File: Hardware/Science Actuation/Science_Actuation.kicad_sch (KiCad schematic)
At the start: 79 parts, among them J2 RJ45_LED_Shielded, SW1 SW_Push, SW2 SW_Push, SW3 SW_Push, SW4 SW_Push, SW5 SW_Push, SW6 SW_Push, SW7 SW_SPDT, U2 OKI, U2 Teensy4.1_DEV-16771, U3 VNH7070AS, U4 VNH7070AS, U5 VNH7070AS, U6 VNH7070AS

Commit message: Add more caps to VNH and expand 12V plane
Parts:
- added C13, C14, C15, C16: 10uF, Capacitor_SMD:C_0603_1608Metric_Pad1.08x0.95mm_HandSolder, symbol Device:C
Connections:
- net +12V: now also C13.1, C14.1, C15.1, C16.1
- net GND: now also C13.2, C14.2, C15.2, C16.2
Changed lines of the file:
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@@
     (stroke (width 0) (type default))
   )
+  (wire (pts (xy 72.39 208.28) (xy 72.39 207.01))
+    (stroke (width 0) (type default))
+  )
   (wire (pts (xy 190.5 156.21) (xy 190.5 157.48))
     (stroke (width 0) (type default))
@@
     (stroke (width 0) (type default))
   )
+  (wire (pts (xy 62.23 102.87) (xy 64.77 102.87))
+    (stroke (width 0) (type default))
+  )
   (wire (pts (xy 27.94 67.31) (xy 46.99 67.31))
     (stroke (width 0) (type default))
@@
     (stroke (width 0) (type default))
   )
+  (wire (pts (xy 73.66 156.21) (xy 73.66 154.94))
+    (stroke (width 0) (type default))
+  )
   (wire (pts (xy 76.2 285.75) (xy 76.2 287.02))
     (stroke (width 0) (type default))
@@
     (stroke (width 0) (type default))
   )
+  (wire (pts (xy 60.96 207.01) (xy 63.5 207.01))
+    (stroke (width 0) (type default))
+  )
   (wire (pts (xy 152.4 267.97) (xy 152.4 276.86))
     (stroke (width 0) (type default))
@@
     (stroke (width 0) (type default))
   )
+  (wire (pts (xy 62.23 154.94) (xy 64.77 154.94))
+    (stroke (width 0) (type default))
+  )
   (wire (pts (xy 143.51 113.03) (xy 146.05 113.03))
     (stroke (width 0) (type default))
@@
     (stroke (width 0) (type default))
   )
+  (wire (pts (xy 72.39 207.01) (xy 71.12 207.01))
+    (stroke (width 0) (type default))
+  )
   (wire (pts (xy 290.83 87.63) (xy 293.37 87.63))
     (stroke (width 0) (type default))
@@
     (stroke (width 0) (type default))
   )
+  (wire (pts (xy 73.66 102.87) (xy 72.39 102.87))
+    (stroke (width 0) (type default))
+  )
   (wire (pts (xy 76.2 233.68) (xy 76.2 234.95))
     (stroke (width 0) (type default))
@@
     (stroke (width 0) (type default))
   )
+  (wire (pts (xy 72.39 259.08) (xy 71.12 259.08))
+    (stroke (width 0) (type default))
+  )
   (wire (pts (xy 189.23 58.42) (xy 190.5 58.42))
     (stroke (width 0) (type default))
   )
+  (wire (pts (xy 73.66 154.94) (xy 72.39 154.94))
+    (stroke (width 0) (type default))
+  )
   (wire (pts (xy 86.36 233.68) (xy 88.9 233.68))
     (stroke (width 0) (type default))
@@
     (stroke (width 0) (type default))
   )
+  (wire (pts (xy 60.96 259.08) (xy 63.5 259.08))
+    (stroke (width 0) (type default))
+  )
   (wire (pts (xy 175.26 267.97) (xy 176.53 267.97))
     (stroke (width 0) (type default))
@@
     (stroke (width 0) (type default))
   )
+  (wire (pts (xy 73.66 104.14) (xy 73.66 102.87))
+    (stroke (width 0) (type default))
+  )
   (wire (pts (xy 104.14 29.21) (xy 104.14 31.75))
     (stroke (width 0) (type default))
@@
     (stroke (width 0) (type default))
   )
+  (wire (pts (xy 72.39 260.35) (xy 72.39 259.08))
+    (stroke (width 0) (type default))
+  )
   (wire (pts (xy 146.05 33.02) (xy 147.32 33.02))
     (stroke (width 0) (type default))
@@
     )
   )
+  (symbol (lib_id "Device:C") (at 68.58 154.94 90) (unit 1)
+    (in_bom yes) (on_board yes) (dnp no) (fields_autoplaced)
+    (property "Reference" "C14" (at 68.58 147.32 90)
+      (effects (font (size 1.27 1.27)))
+    )
+    (property "Value" "10uF" (at 68.58 149.86 90)
+      (effects (font (size 1.27 1.27)))
+    )
+    (property "Footprint" "Capacitor_SMD:C_0603_1608Metric_Pad1.08x0.95mm_HandSolder" (at 72.39 153.9748 0)
+      (effects (font (size 1.27 1.27)) hide)
+    )
+    (property "Datasheet" "~" (at 68.58 154.94 0)
+      (effects (font (size 1.27 1.27)) hide)
+    )
+    (pin "1")
+    (pin "2")
+    (instances
+      (project "Science_Actuation"
+        (path "/a309c31d-a907-45c3-9170-b69a69763088"
+          (reference "C14") (unit 1)
+        )
+      )
+    )
+  )
   (symbol (lib_id "Device:LED") (at 93.98 45.72 90) (unit 1)
     (in_bom yes) (on_board yes) (dnp no) (fields_autoplaced)
@@
     )
   )
+  (symbol (lib_id "Device:C") (at 67.31 207.01 90) (unit 1)
+    (in_bom yes) (on_board yes) (dnp no) (fields_autoplaced)
+    (property "Reference" "C15" (at 67.31 199.39 90)
+      (effects (font (size 1.27 1.27)))
+    )
+    (property "Value" "10uF" (at 67.31 201.93 90)
+      (effects (font (size 1.27 1.27)))
+    )
+    (property "Footprint" "Capacitor_SMD:C_0603_1608Metric_Pad1.08x0.95mm_HandSolder" (at 71.12 206.0448 0)
+      (effects (font (size 1.27 1.27)) hide)
+    )
+    (property "Datasheet" "~" (at 67.31 207.01 0)
+      (effects (font (size 1.27 1.27)) hide)
+    )
+    (pin "1")
+    (pin "2")
+    (instances
+      (project "Science_Actuation"
+        (path "/a309c31d-a907-45c3-9170-b69a69763088"
+          (reference "C15") (unit 1)
+        )
+      )
+    )
+  )
   (symbol (lib_id "Device:R") (at 44.45 165.1 90) (unit 1)
     (in_bom yes) (on_board yes) (dnp no)
@@
     )
   )
+  (symbol (lib_id "power:GND") (at 72.39 208.28 0) (unit 1)
+    (in_bom yes) (on_board yes) (dnp no) (fields_autoplaced)
+    (property "Reference" "#PWR036" (at 72.39 214.63 0)
+      (effects (font (size 1.27 1.27)) hide)
+    )
+    (property "Value" "GND" (at 72.39 213.36 0)
+      (effects (font (size 1.27 1.27)))
+    )
+    (property "Footprint" "" (at 72.39 208.28 0)
+      (effects (font (size 1.27 1.27)) hide)
+    )
+    (property "Datasheet" "" (at 72.39 208.28 0)
+      (effects (font (size 1.27 1.27)) hide)
+    )
+    (pin "1")
+    (instances
+      (project "Science_Actuation"
+        (path "/a309c31d-a907-45c3-9170-b69a69763088"
+          (reference "#PWR036") (unit 1)
+        )
+      )
+    )
+  )
   (symbol (lib_id "Device:R") (at 83.82 129.54 90) (unit 1)
     (in_bom yes) (on_board yes) (dnp no)
@@
     )
   )
+  (symbol (lib_id "Device:C") (at 68.58 102.87 90) (unit 1)
+    (in_bom yes) (on_board yes) (dnp no) (fields_autoplaced)
+    (property "Reference" "C13" (at 68.58 95.25 90)
+      (effects (font (size 1.27 1.27)))
+    )
+    (property "Value" "10uF" (at 68.58 97.79 90)
+      (effects (font (size 1.27 1.27)))
+    )
+    (property "Footprint" "Capacitor_SMD:C_0603_1608Metric_Pad1.08x0.95mm_HandSolder" (at 72.39 101.9048 0)
+      (effects (font (size 1.27 1.27)) hide)
+    )
+    (property "Datasheet" "~" (at 68.58 102.87 0)
+      (effects (font (size 1.27 1.27)) hide)
+    )
+    (pin "1")
+    (pin "2")
+    (instances
+      (project "Science_Actuation"
+        (path "/a309c31d-a907-45c3-9170-b69a69763088"
+          (reference "C13") (unit 1)
+        )
+      )
+    )
+  )
   (symbol (lib_id "MRDT_Connectors:AndersonPP") (at 21.59 46.99 0) (unit 1)
     (in_bom yes) (on_board yes) (dnp no) (fields_autoplaced)
@@
     )
   )
+  (symbol (lib_id "Device:C") (at 67.31 259.08 90) (unit 1)
+    (in_bom yes) (on_board yes) (dnp no) (fields_autoplaced)
+    (property "Reference" "C16" (at 67.31 251.46 90)
+      (effects (font (size 1.27 1.27)))
+    )
+    (property "Value" "10uF" (at 67.31 254 90)
+      (effects (font (size 1.27 1.27)))
+    )
+    (property "Footprint" "Capacitor_SMD:C_0603_1608Metric_Pad1.08x0.95mm_HandSolder" (at 71.12 258.1148 0)
+      (effects (font (size 1.27 1.27)) hide)
+    )
+    (property "Datasheet" "~" (at 67.31 259.08 0)
+      (effects (font (size 1.27 1.27)) hide)
+    )
+    (pin "1")
+    (pin "2")
+    (instances
+      (project "Science_Actuation"
+        (path "/a309c31d-a907-45c3-9170-b69a69763088"
+          (reference "C16") (unit 1)
+        )
+      )
+    )
+  )
   (symbol (lib_id "power:GND") (at 46.99 208.28 0) (unit 1)
     (in_bom yes) (on_board yes) (dnp no) (fields_autoplaced)
@@
     )
   )
+  (symbol (lib_id "power:GND") (at 73.66 104.14 0) (unit 1)
+    (in_bom yes) (on_board yes) (dnp no) (fields_autoplaced)
+    (property "Reference" "#PWR034" (at 73.66 110.49 0)
+      (effects (font (size 1.27 1.27)) hide)
+    )
+    (property "Value" "GND" (at 73.66 109.22 0)
+      (effects (font (size 1.27 1.27)))
+    )
+    (property "Footprint" "" (at 73.66 104.14 0)
+      (effects (font (size 1.27 1.27)) hide)
+    )
+    (property "Datasheet" "" (at 73.66 104.14 0)
+      (effects (font (size 1.27 1.27)) hide)
+    )
+    (pin "1")
+    (instances
+      (project "Science_Actuation"
+        (path "/a309c31d-a907-45c3-9170-b69a69763088"
+          (reference "#PWR034") (unit 1)
+        )
+      )
+    )
+  )
   (symbol (lib_id "power:GND") (at 46.99 260.35 0) (unit 1)
     (in_bom yes) (on_board yes) (dnp no) (fields_autoplaced)
@@
     )
   )
+  (symbol (lib_id "power:GND") (at 72.39 260.35 0) (unit 1)
+    (in_bom yes) (on_board yes) (dnp no) (fields_autoplaced)
+    (property "Reference" "#PWR037" (at 72.39 266.7 0)
+      (effects (font (size 1.27 1.27)) hide)
+    )
+    (property "Value" "GND" (at 72.39 265.43 0)
+      (effects (font (size 1.27 1.27)))
+    )
+    (property "Footprint" "" (at 72.39 260.35 0)
+      (effects (font (size 1.27 1.27)) hide)
+    )
+    (property "Datasheet" "" (at 72.39 260.35 0)
+      (effects (font (size 1.27 1.27)) hide)
+    )
+    (pin "1")
+    (instances
+      (project "Science_Actuation"
+        (path "/a309c31d-a907-45c3-9170-b69a69763088"
+          (reference "#PWR037") (unit 1)
+        )
+      )
+    )
+  )
   (symbol (lib_id "Switch:SW_Push") (at 157.48 212.09 0) (unit 1)
     (in_bom yes) (on_board yes) (dnp no) (fields_autoplaced)
@@
         )
       )
+    )
+  )
+  (symbol (lib_id "power:GND") (at 73.66 156.21 0) (unit 1)
+    (in_bom yes) (on_board yes) (dnp no) (fields_autoplaced)
+    (property "Reference" "#PWR035" (at 73.66 162.56 0)
+      (effects (font (size 1.27 1.27)) hide)
+    )
+    (property "Value" "GND" (at 73.66 161.29 0)
+      (effects (font (size 1.27 1.27)))
+    )
+    (property "Footprint" "" (at 73.66 156.21 0)
+      (effects (font (size 1.27 1.27)) hide)
+    )
+    (property "Datasheet" "" (at 73.66 156.21 0)
+      (effects (font (size 1.27 1.27)) hide)
+    )
+    (pin "1")
+    (instances
+      (project "Science_Actuation"
+        (path "/a309c31d-a907-45c3-9170-b69a69763088"
+          (reference "#PWR035") (unit 1)
+        )
+      )

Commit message: Review changes and regenerate gerbs
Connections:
- net GND: now also C3.1, J2.SH
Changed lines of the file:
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@@
   (junction (at 48.26 130.81) (diameter 0) (color 0 0 0 0)
   )
+  (junction (at 248.92 227.33) (diameter 0) (color 0 0 0 0)
+  )
   (junction (at 59.69 44.45) (diameter 0) (color 0 0 0 0)
   )
@@
     (stroke (width 0) (type default))
   )
+  (wire (pts (xy 248.92 227.33) (xy 248.92 228.6))
+    (stroke (width 0) (type default))
+  )
   (wire (pts (xy 247.65 77.47) (xy 250.19 77.47))
     (stroke (width 0) (type default))
@@
         )
       )
+    )
+  )
+  (symbol (lib_id "power:GND") (at 248.92 228.6 0) (unit 1)
+    (in_bom yes) (on_board yes) (dnp no) (fields_autoplaced)
+    (property "Reference" "#PWR053" (at 248.92 234.95 0)
+      (effects (font (size 1.27 1.27)) hide)
+    )
+    (property "Value" "GND" (at 248.92 233.68 0)
+      (effects (font (size 1.27 1.27)))
+    )
+    (property "Footprint" "" (at 248.92 228.6 0)
+      (effects (font (size 1.27 1.27)) hide)
+    )
+    (property "Datasheet" "" (at 248.92 228.6 0)
+      (effects (font (size 1.27 1.27)) hide)
+    )
+    (pin "1")
+    (instances
+      (project "Science_Actuation"
+        (path "/a309c31d-a907-45c3-9170-b69a69763088"
+          (reference "#PWR053") (unit 1)
+        )
+      )

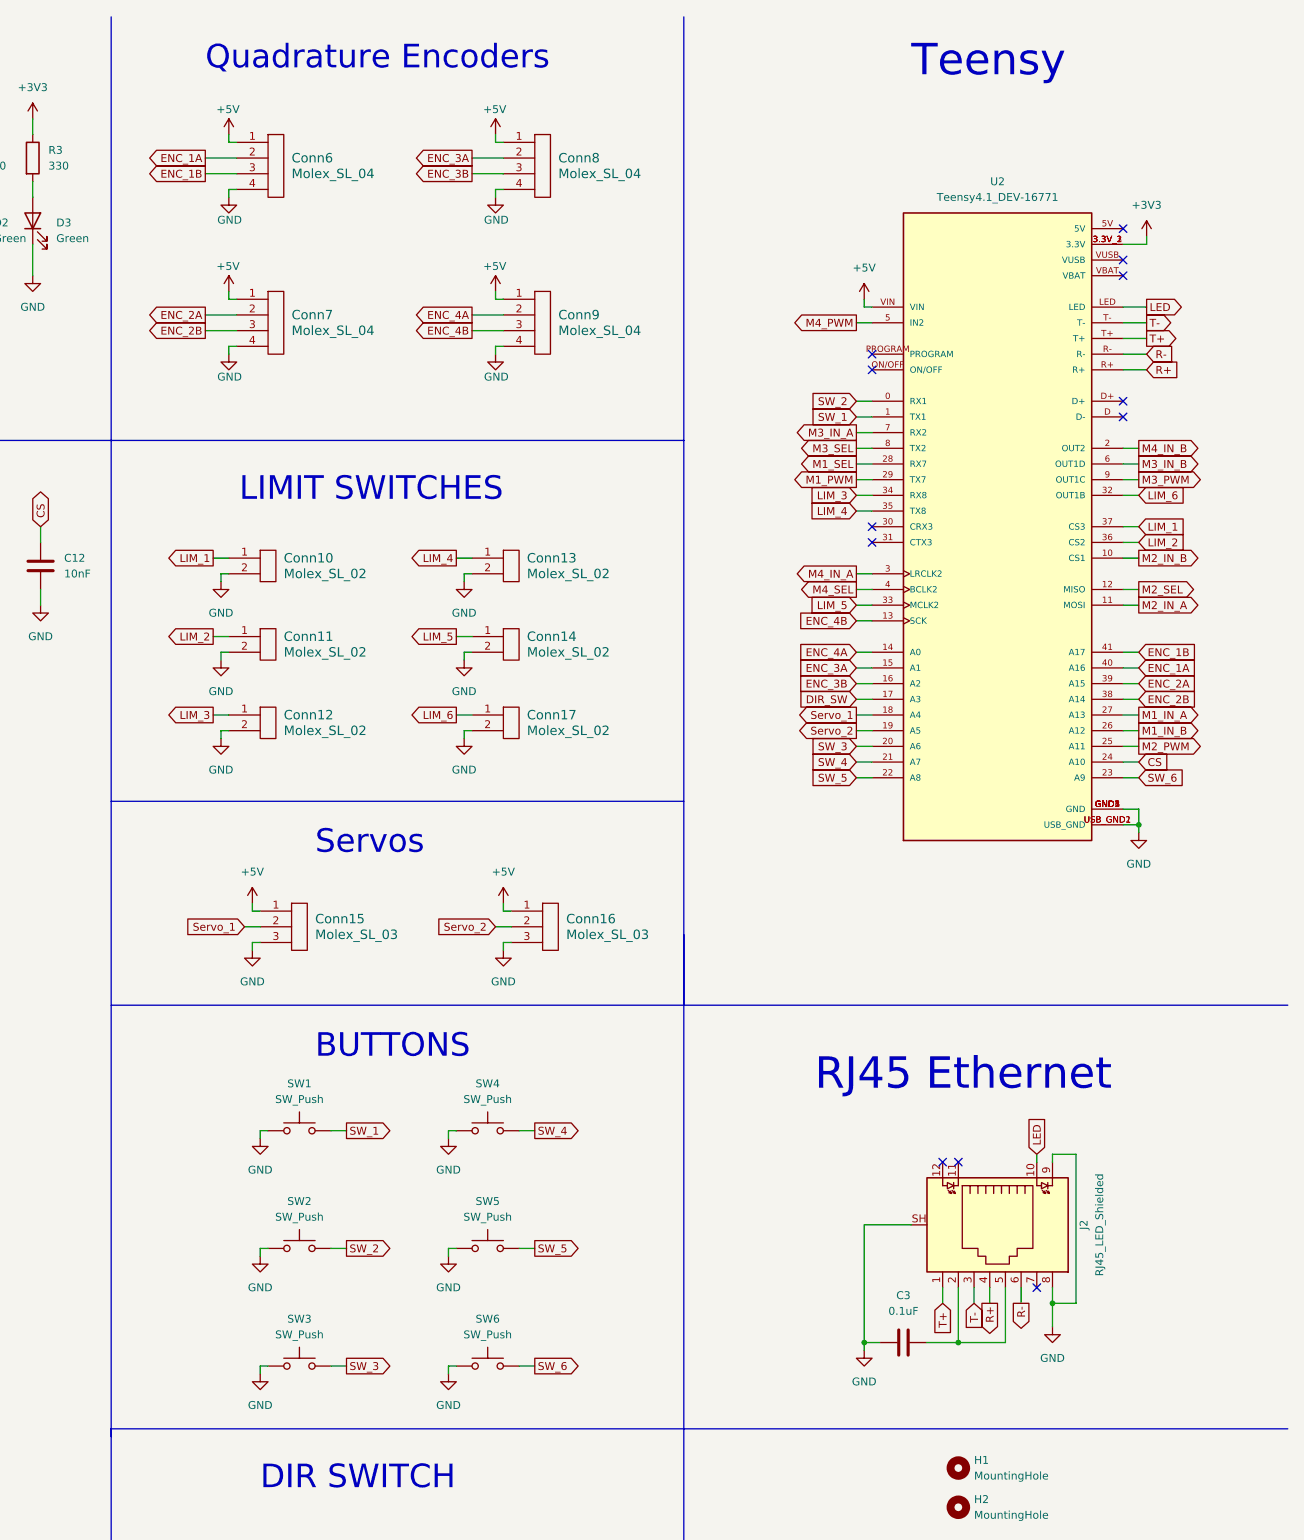
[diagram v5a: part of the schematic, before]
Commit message: Add temp and humidity sensor
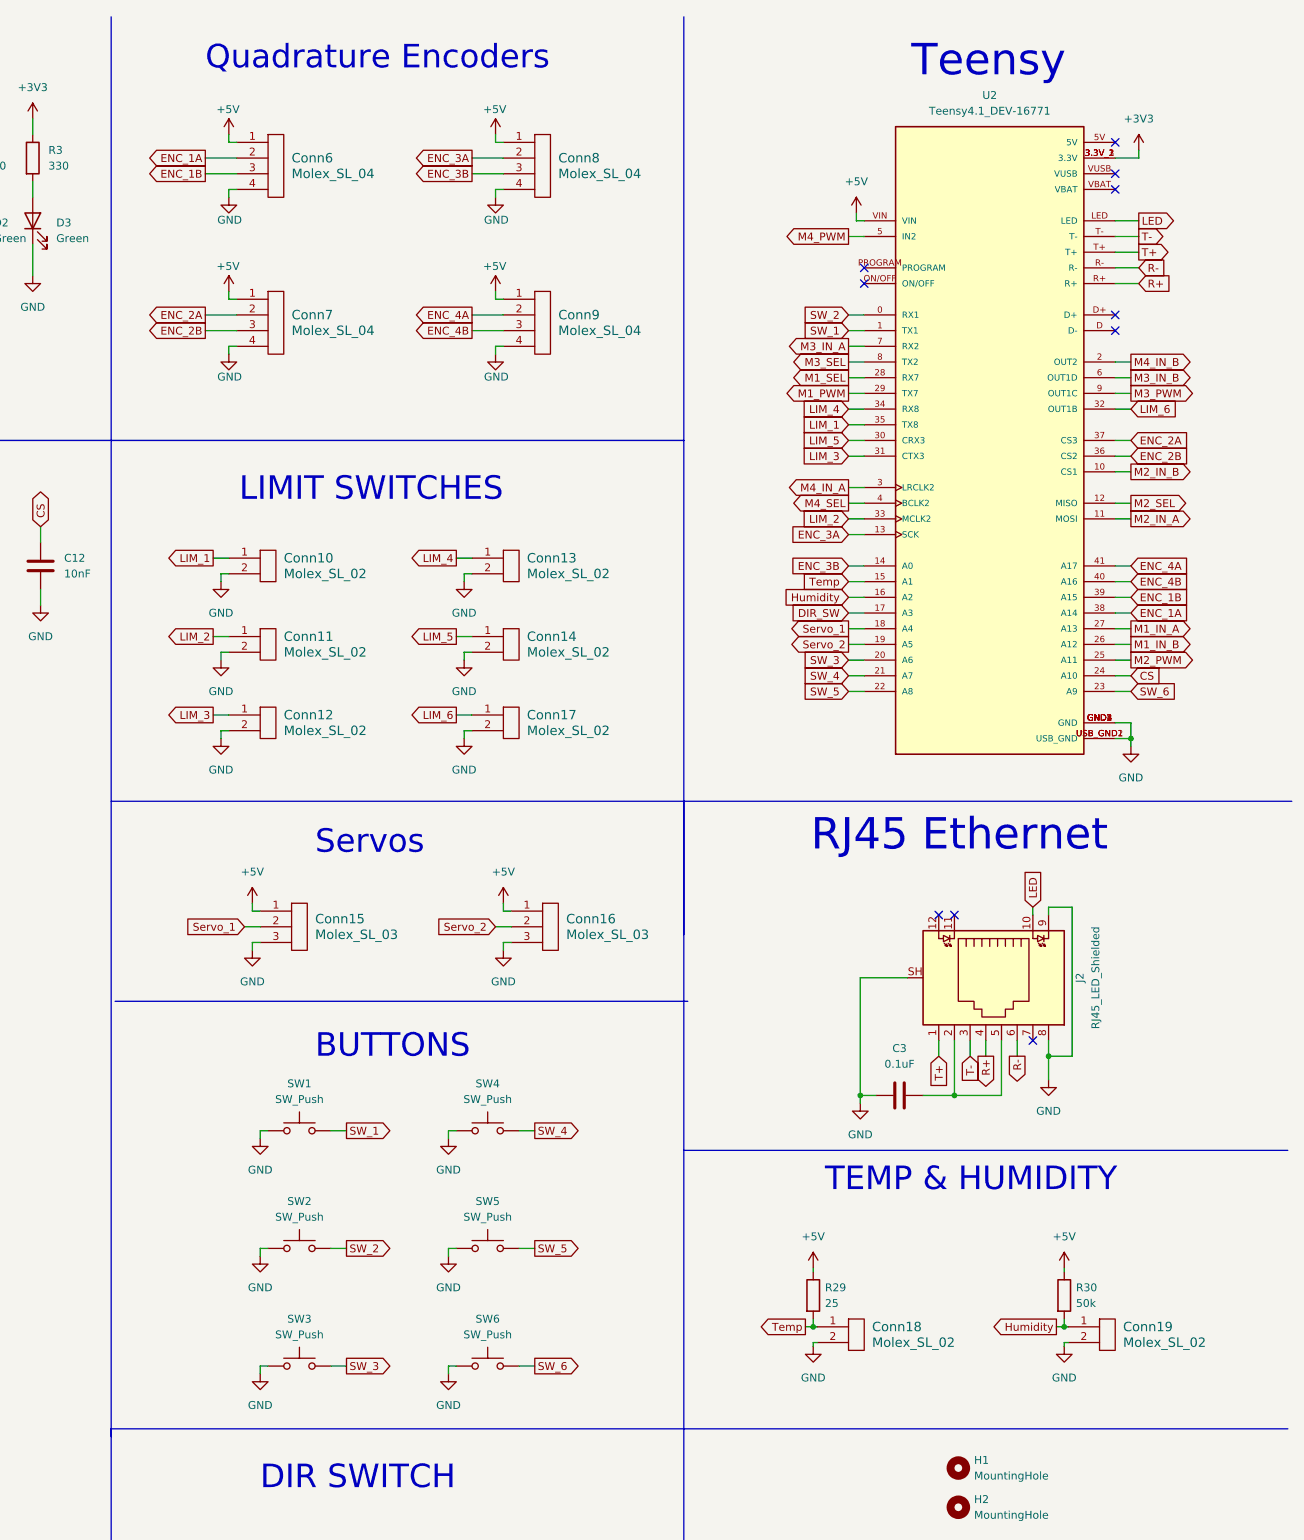
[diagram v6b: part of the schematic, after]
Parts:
- added Conn18, Conn19: Molex_SL_02, MRDT_Connectors:MOLEX_SL_02_Vertical, symbol MRDT_Connectors:Molex_SL_02
- added R29: 25, Resistor_SMD:R_0603_1608Metric_Pad0.98x0.95mm_HandSolder, symbol Device:R
- added R30: 50k, Resistor_SMD:R_0603_1608Metric_Pad0.98x0.95mm_HandSolder, symbol Device:R
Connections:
- net +5V: now also R29.1, R30.1
- net ENC_1A: now also U2.38 (A14); no longer U2.40 (A16)
- net ENC_1B: now also U2.39 (A15); no longer U2.41 (A17)
- net ENC_2A: now also U2.37 (CS3); no longer U2.39 (A15)
- net ENC_2B: now also U2.36 (CS2); no longer U2.38 (A14)
- net ENC_3A: now also U2.13 (SCK); no longer U2.15 (A1)
- net ENC_3B: now also U2.14 (A0); no longer U2.16 (A2)
- net ENC_4A: now also U2.41 (A17); no longer U2.14 (A0)
- net ENC_4B: now also U2.40 (A16); no longer U2.13 (SCK)
- net GND: now also Conn18.2, Conn19.2
- net LIM_1: now also U2.35 (TX8); no longer U2.37 (CS3)
- net LIM_2: now also U2.33 (MCLK2); no longer U2.36 (CS2)
- net LIM_3: now also U2.31 (CTX3); no longer U2.34 (RX8)
- net LIM_4: now also U2.34 (RX8); no longer U2.35 (TX8)
- net LIM_5: now also U2.30 (CRX3); no longer U2.33 (MCLK2)
- new net Humidity: Conn19.1, R30.2, U2.16 (A2)
- new net Temp: Conn18.1, R29.2, U2.15 (A1)
- no-connect marks 12 -> 10
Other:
- note added: "TEMP & HUMIDITY"
- moved on the sheet: C3, J2, U2
